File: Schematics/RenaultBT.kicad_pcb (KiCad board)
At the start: 2 copper layers, 11 parts, among them Q1 2N7000, U1 LM2576T-5, U2 LM1117-3.3

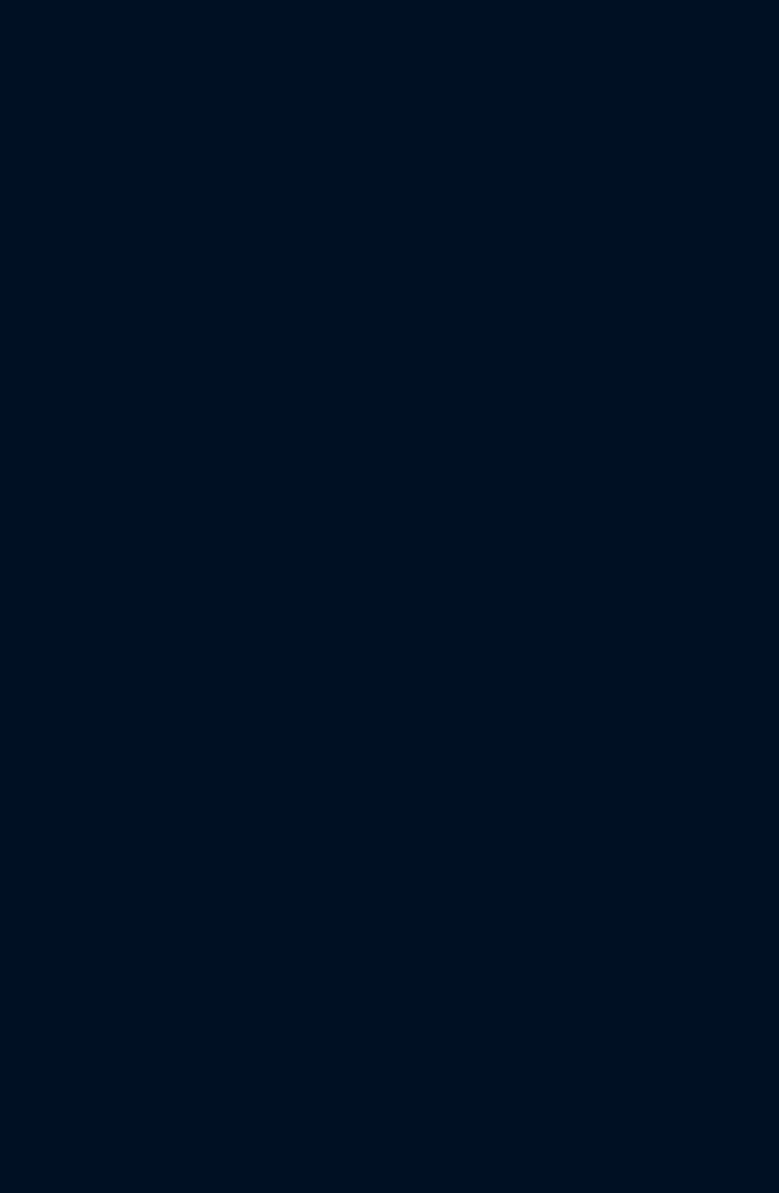
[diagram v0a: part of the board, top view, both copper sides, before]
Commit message: Added WM8804 library
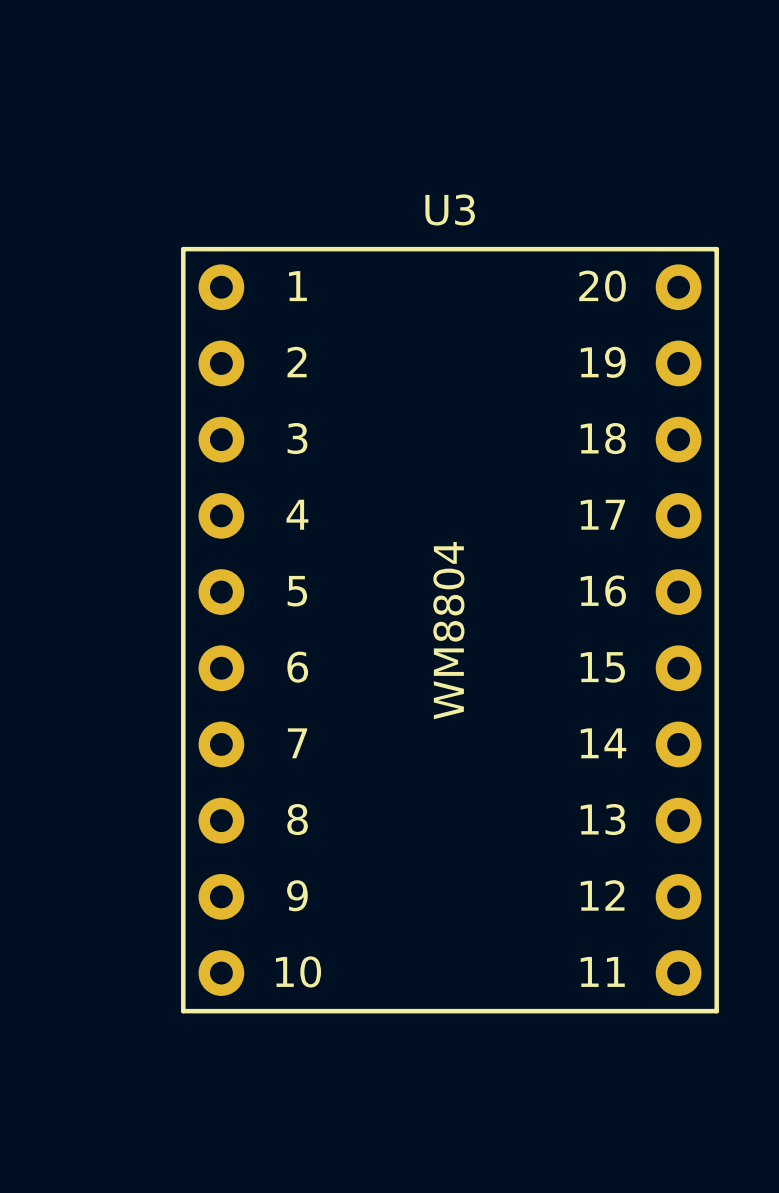
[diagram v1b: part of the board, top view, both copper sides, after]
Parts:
- added U3: WM8804, WM8804:WM8804_Breakout_18mm_x_25mm, F.Cu at (180.3, 85.1)
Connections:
- net 12V renamed /PowerSupply/12V
- net 3V3 renamed /PowerSupply/3V3
- net 5V renamed /PowerSupply/5V
- net GND renamed /PowerSupply/GND
- net HU_ON renamed /PowerSupply/HU_ON

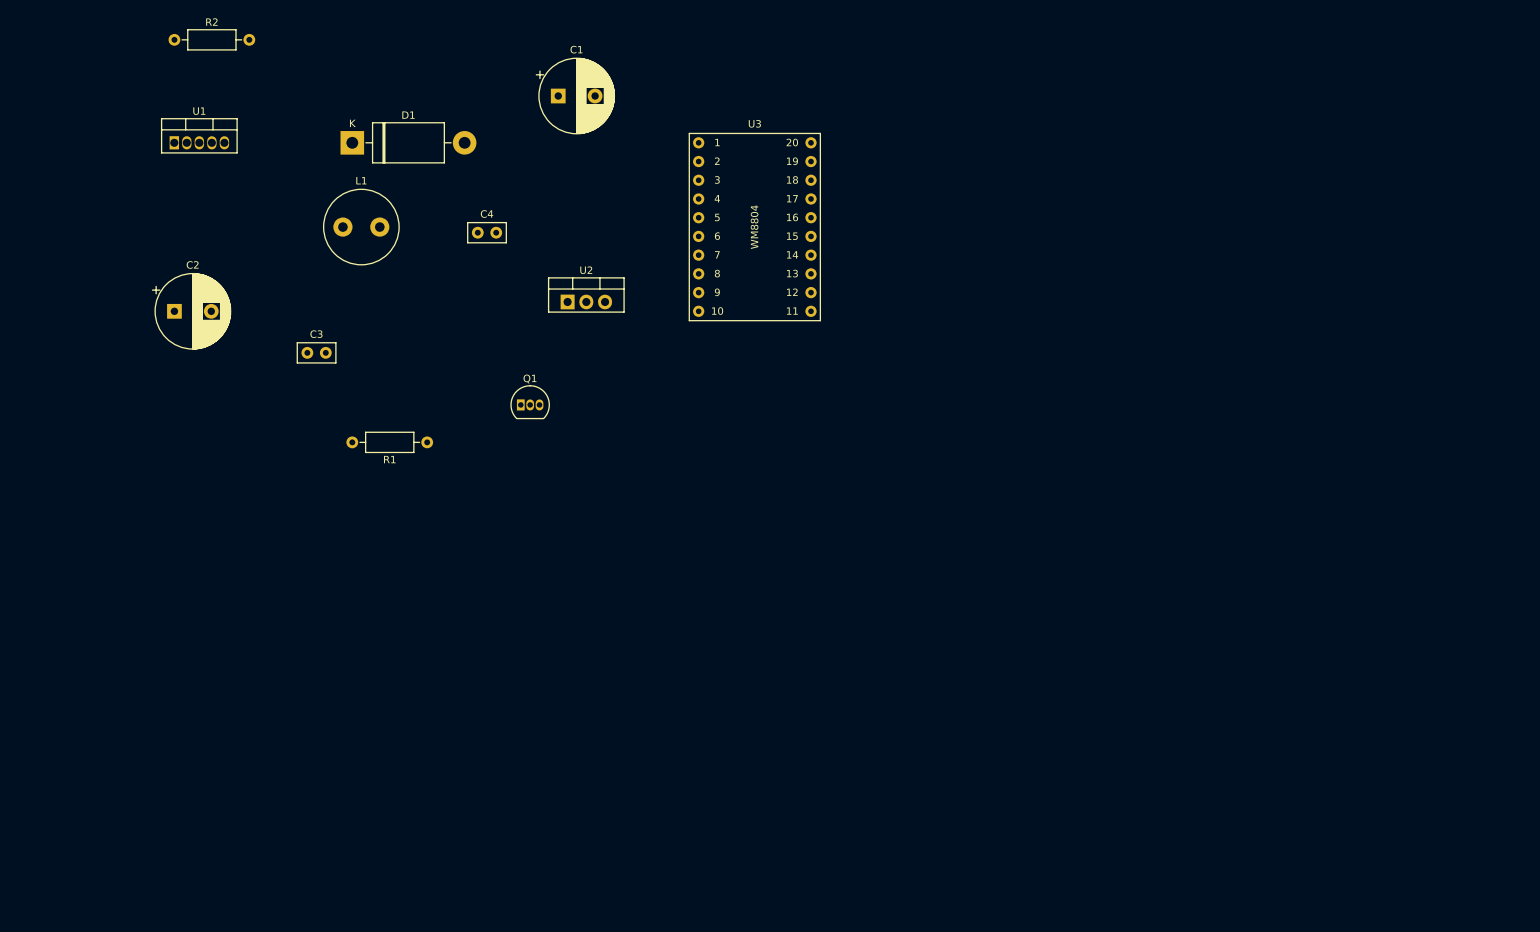
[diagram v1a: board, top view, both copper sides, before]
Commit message: Added BT module, HU-CDC interface adapter, I2S to SPDIF converter, SPDIF interface and main controller to the schematics
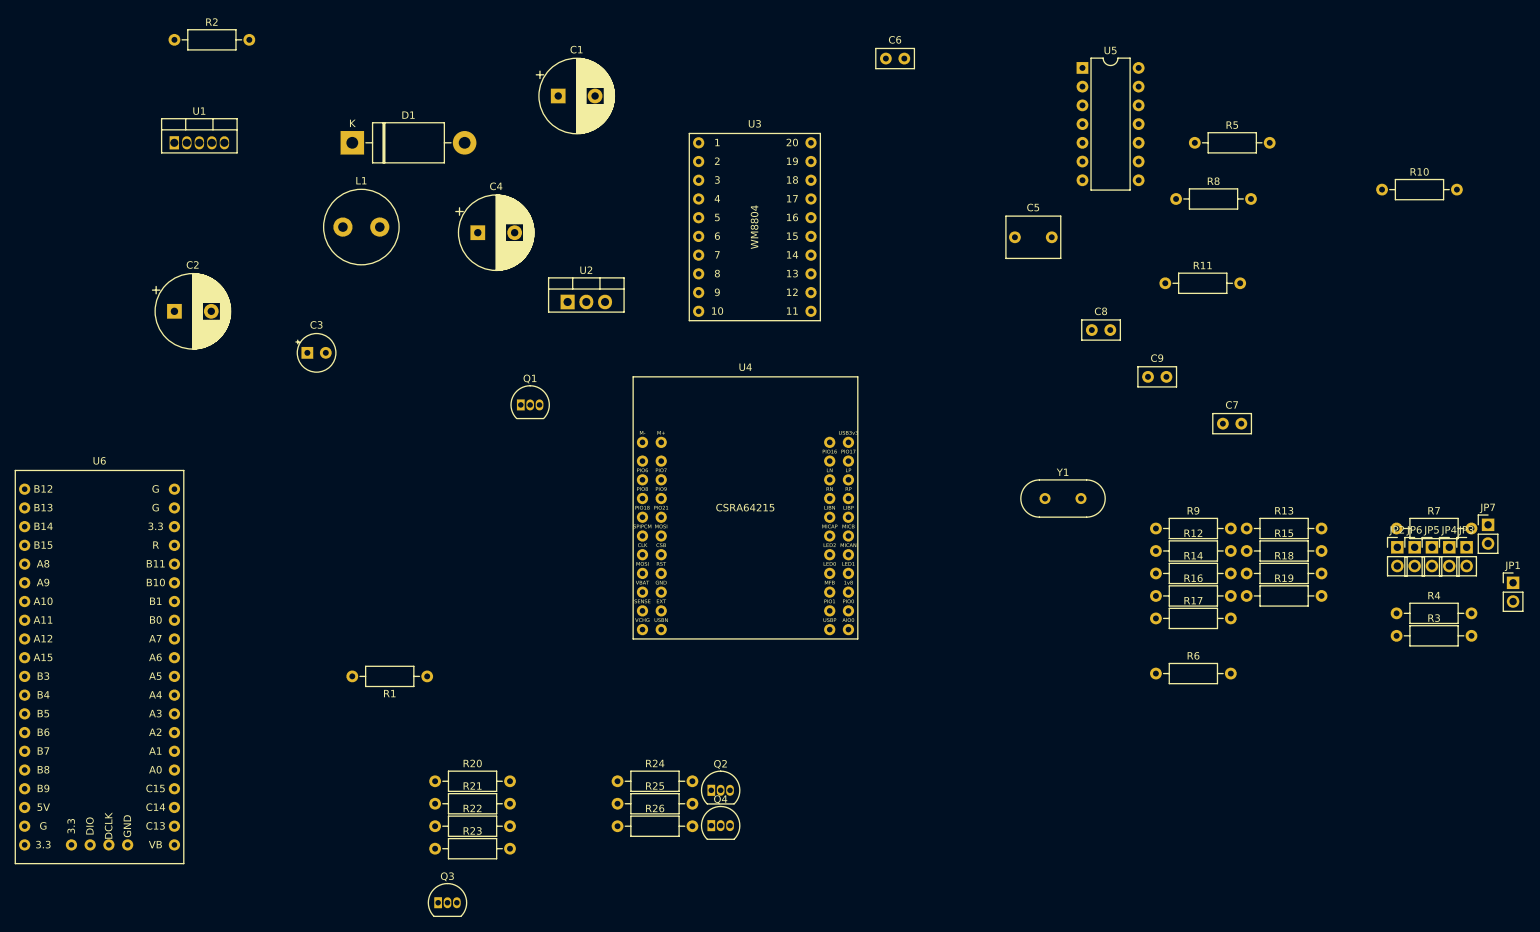
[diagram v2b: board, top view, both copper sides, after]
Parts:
- added C5: 1uF, Capacitor_THT:C_Rect_L7.2mm_W5.5mm_P5.00mm_FKS2_FKP2_MKS2_MKP2, F.Cu at (215.6, 86.5)
- added C6: 15pF, Capacitor_THT:C_Disc_D5.0mm_W2.5mm_P2.50mm, F.Cu at (198.1, 62.2)
- added C7: 15pF, Capacitor_THT:C_Disc_D5.0mm_W2.5mm_P2.50mm, F.Cu at (243.8, 111.8)
- added C8: 0.1uF, Capacitor_THT:C_Disc_D5.0mm_W2.5mm_P2.50mm, F.Cu at (226.1, 99.1)
- added C9: 150n, Capacitor_THT:C_Disc_D5.0mm_W2.5mm_P2.50mm, F.Cu at (233.7, 105.4)
- added JP1: Jumper, Connector_PinHeader_2.54mm:PinHeader_1x02_P2.54mm_Vertical, F.Cu at (283.2, 133.3)
- added JP2: Jumper, Connector_PinHeader_2.54mm:PinHeader_1x02_P2.54mm_Vertical, F.Cu at (267.5, 128.5)
- added JP3: Jumper, Connector_PinHeader_2.54mm:PinHeader_1x02_P2.54mm_Vertical, F.Cu at (276.9, 128.5)
- added JP4: Jumper, Connector_PinHeader_2.54mm:PinHeader_1x02_P2.54mm_Vertical, F.Cu at (274.6, 128.5)
- added JP5: Jumper, Connector_PinHeader_2.54mm:PinHeader_1x02_P2.54mm_Vertical, F.Cu at (272.2, 128.5)
- added JP6: Jumper, Connector_PinHeader_2.54mm:PinHeader_1x02_P2.54mm_Vertical, F.Cu at (269.9, 128.5)
- added JP7: Jumper, Connector_PinHeader_2.54mm:PinHeader_1x02_P2.54mm_Vertical, F.Cu at (279.8, 125.5)
- added Q2: 2N7000, Package_TO_SOT_THT:TO-92_Inline, F.Cu at (174.4, 161.5)
- added Q3: 2N7000, Package_TO_SOT_THT:TO-92_Inline, F.Cu at (137.4, 176.8)
- added Q4: 2N7000, Package_TO_SOT_THT:TO-92_Inline, F.Cu at (174.4, 166.3)
- added R10: 10k, Resistor_THT:R_Axial_DIN0207_L6.3mm_D2.5mm_P10.16mm_Horizontal, F.Cu at (265.4, 80.0)
- added R11: 10k, Resistor_THT:R_Axial_DIN0207_L6.3mm_D2.5mm_P10.16mm_Horizontal, F.Cu at (236.0, 92.7)
- added R12: 10k, Resistor_THT:R_Axial_DIN0207_L6.3mm_D2.5mm_P10.16mm_Horizontal, F.Cu at (234.8, 129.0)
- added R13: 10k, Resistor_THT:R_Axial_DIN0207_L6.3mm_D2.5mm_P10.16mm_Horizontal, F.Cu at (247.1, 126.0)
- added R14: 12k, Resistor_THT:R_Axial_DIN0207_L6.3mm_D2.5mm_P10.16mm_Horizontal, F.Cu at (234.8, 132.1)
- added R15: 12k, Resistor_THT:R_Axial_DIN0207_L6.3mm_D2.5mm_P10.16mm_Horizontal, F.Cu at (247.1, 129.0)
- added R16: 12k, Resistor_THT:R_Axial_DIN0207_L6.3mm_D2.5mm_P10.16mm_Horizontal, F.Cu at (234.8, 135.1)
- added R17: 12k, Resistor_THT:R_Axial_DIN0207_L6.3mm_D2.5mm_P10.16mm_Horizontal, F.Cu at (234.8, 138.2)
- added R18: 12k, Resistor_THT:R_Axial_DIN0207_L6.3mm_D2.5mm_P10.16mm_Horizontal, F.Cu at (247.1, 132.1)
- added R19: 12k, Resistor_THT:R_Axial_DIN0207_L6.3mm_D2.5mm_P10.16mm_Horizontal, F.Cu at (247.1, 135.1)
- added R20: 4.7K, Resistor_THT:R_Axial_DIN0207_L6.3mm_D2.5mm_P10.16mm_Horizontal, F.Cu at (137.0, 160.3)
- added R21: 4.7K, Resistor_THT:R_Axial_DIN0207_L6.3mm_D2.5mm_P10.16mm_Horizontal, F.Cu at (137.0, 163.3)
- added R22: 4.7K, Resistor_THT:R_Axial_DIN0207_L6.3mm_D2.5mm_P10.16mm_Horizontal, F.Cu at (137.0, 166.4)
- added R23: 4.7K, Resistor_THT:R_Axial_DIN0207_L6.3mm_D2.5mm_P10.16mm_Horizontal, F.Cu at (137.0, 169.4)
- added R24: 100, Resistor_THT:R_Axial_DIN0207_L6.3mm_D2.5mm_P10.16mm_Horizontal, F.Cu at (161.7, 160.3)
- added R25: 1K, Resistor_THT:R_Axial_DIN0207_L6.3mm_D2.5mm_P10.16mm_Horizontal, F.Cu at (161.7, 163.3)
- added R26: 47K, Resistor_THT:R_Axial_DIN0207_L6.3mm_D2.5mm_P10.16mm_Horizontal, F.Cu at (161.7, 166.4)
- added R3: 10k, Resistor_THT:R_Axial_DIN0207_L6.3mm_D2.5mm_P10.16mm_Horizontal, F.Cu at (267.4, 140.5)
- added R4: 10K, Resistor_THT:R_Axial_DIN0207_L6.3mm_D2.5mm_P10.16mm_Horizontal, F.Cu at (267.4, 137.5)
- added R5: 374, Resistor_THT:R_Axial_DIN0207_L6.3mm_D2.5mm_P10.16mm_Horizontal, F.Cu at (240.0, 73.7)
- added R6: 93, Resistor_THT:R_Axial_DIN0207_L6.3mm_D2.5mm_P10.16mm_Horizontal, F.Cu at (234.8, 145.7)
- added R7: 10k, Resistor_THT:R_Axial_DIN0207_L6.3mm_D2.5mm_P10.16mm_Horizontal, F.Cu at (267.4, 126.0)
- added R8: 10k, Resistor_THT:R_Axial_DIN0207_L6.3mm_D2.5mm_P10.16mm_Horizontal, F.Cu at (237.5, 81.3)
- added R9: 10k, Resistor_THT:R_Axial_DIN0207_L6.3mm_D2.5mm_P10.16mm_Horizontal, F.Cu at (234.8, 126.0)
- added U4: CSRA64215, CSRA64215:CSRA64215, F.Cu at (179.1, 123.2)
- added U5: 74HC04, Package_DIP:DIP-14_W7.62mm, F.Cu at (224.8, 63.5)
- added U6: STM32F103, STM32:STM32F103C8T6, F.Cu at (91.4, 144.8)
- added Y1: 12Mhz, Crystal:Crystal_HC49-4H_Vertical, F.Cu at (219.7, 121.9)
- C3: value 100nF -> 10uF; footprint Capacitor_THT:C_Disc_D5.0mm_W2.5mm_P2.50mm -> Capacitor_THT:CP_Radial_Tantal_D5.0mm_P2.50mm
- C4: value 10uF -> 100uF; footprint Capacitor_THT:C_Disc_D5.0mm_W2.5mm_P2.50mm -> Capacitor_THT:CP_Radial_D10.0mm_P5.00mm
- moved R1 31.8 mm to (135.9, 146.1)
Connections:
- net Net-(Q1-Pad3) renamed PWR_ON
- C1 pad 2: /PowerSupply/GND -> /I2SToSPDIF/DGND
- C2 pad 2: /PowerSupply/GND -> /I2SToSPDIF/DGND
- C3 pad 2: /PowerSupply/GND -> /I2SToSPDIF/DGND
- C4 pad 1: /PowerSupply/3V3 -> /HU_CDC_InterfaceAdapter/3V3
- C4 pad 2: /PowerSupply/GND -> /I2SToSPDIF/DGND
- D1 pad 2: /PowerSupply/GND -> /I2SToSPDIF/DGND
- Q1 pad 1: /PowerSupply/GND -> /I2SToSPDIF/DGND
- R1 pad 2: /PowerSupply/GND -> /I2SToSPDIF/DGND
- U1 pad 3: /PowerSupply/GND -> /I2SToSPDIF/DGND
- U2 pad 1: /PowerSupply/GND -> /I2SToSPDIF/DGND
- U2 pad 2: /PowerSupply/3V3 -> /HU_CDC_InterfaceAdapter/3V3
- U3 pad 1: Net-(U3-Pad1) -> /MainController/I2C1_SCL
- U3 pad 12: Net-(U3-Pad12) -> (no net)
- U3 pad 13: Net-(U3-Pad13) -> /I2SToSPDIF/I2S_SD_IN
- U3 pad 14: Net-(U3-Pad14) -> /BTModule/I2S_CLK
- U3 pad 15: Net-(U3-Pad15) -> /BTModule/I2S_WS
- U3 pad 16: Net-(U3-Pad16) -> (no net)
- U3 pad 17: Net-(U3-Pad17) -> /I2SToSPDIF/SPDIFOutput_buffered/SPDIF_TTL
- U3 pad 18: Net-(U3-Pad18) -> /I2SToSPDIF/DGND
- U3 pad 19: Net-(U3-Pad19) -> /HU_CDC_InterfaceAdapter/3V3
- U3 pad 2: Net-(U3-Pad2) -> /I2SToSPDIF/DGND
- U3 pad 20: Net-(U3-Pad20) -> (no net)
- U3 pad 3: Net-(U3-Pad3) -> /MainController/I2C1_SDA
- U3 pad 4: Net-(U3-Pad4) -> (no net)
- U3 pad 7: Net-(U3-Pad7) -> /HU_CDC_InterfaceAdapter/3V3
- U3 pad 8: Net-(U3-Pad8) -> /I2SToSPDIF/DGND
- U3 pad 9: Net-(U3-Pad9) -> (no net)
